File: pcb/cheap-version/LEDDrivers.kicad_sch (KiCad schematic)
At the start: 54 parts, among them J711 LED +/- (return isolated), J721 LED +/- (return isolated), J731 LED +/- (return isolated), Q711 AOD66923, Q721 AOD66923, U700 SN74LVC1G08DBVR, U710 AL8853S-13, U720 AL8853S-13

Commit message: cheap-version: schematic substitutions from stock parts
tools/make_cheap1.py generates the cheap-1 sheets from the PCB_V1 0.22 baseline:
ST1S14 for LMR16020 (RT resistor removed, EN/FB divider recalculated), IRS4427S and
IRL2505 for the heater, BSC146N10LS5 for the LED boost switches, SS56 diodes,
KF301/FS1.5/KF2510/XH connectors, stock resistors and capacitors (Source field =
stock:<id>). J901 XT60 is replaced by a screw terminal as decided. U101 TPS54202 and
D711/D721 SS5P10 are kept because datasheets for ST1S10 and SBRT15U100SP5 were not
available. ERC: 0 errors (one warning: footprint for the DTMSS-27 inductor pending);
netdiff against PCB_V1: no connectivity differences among untouched pins.

Co-Authored-By: Claude Sonnet 5.5 <noreply@anthropic.com>
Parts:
- C700: Source (none) -> stock:54
- C710, C715, C725: LCSC C386166 -> C92388; MPN UMK325AB7106KMHP -> CL32B106KBJNNNE; Manufacturer Taiyo Yuden -> Samsung Electro-Mechanics; Source (none) -> stock:47
- C711, C721: value 1u 50V X7R -> 2.2u 50V X7R; footprint Capacitor_SMD:C_0805_2012Metric -> Capacitor_SMD:C_1206_3216Metric; LCSC C28323 -> (none); MPN CL21B105KBFNNNE -> 12065C225KATM-HW; Manufacturer Samsung -> KYOCERA AVX; Source (none) -> stock:3
- C716, C717, C718, C719, C726, C727, C728: value 10u 100V X7S -> 4.7u 100V X7R; LCSC C576517 -> (none); MPN GRM32EC72A106KE05L -> CL32B475KCI6PJE; Manufacturer Murata -> Samsung Electro-Mechanics; Source (none) -> stock:2
- J711, J721, J731: footprint GrowBox:TerminalBlock_KANGNEX_WJ500V-5.08_1x02_P5.08mm_Horizontal -> TerminalBlock_Phoenix:TerminalBlock_Phoenix_MKDS-1,5-2_1x02_P5.00mm_Horizontal; LCSC C8465 -> (none); MPN WJ500V-5.08-2P -> KF301-5.0-2P; Manufacturer KANGNEX -> (none); Source (none) -> stock:93
- L711: value 47u SRP1770TA-470M -> 47u DTMSS-27/0.047/15-V; footprint Inductor_SMD:L_Bourns_SRP1770TA_16.9x16.9mm -> GrowBox:L_Feryster_DTMSS-27_THT; LCSC C2041872 -> (none); MPN SRP1770TA-470M -> DTMSS-27/0.047/15-V; Manufacturer Bourns -> Feryster; Source (none) -> stock:12
- Q711, Q721: value AOD66923 -> BSC146N10LS5; footprint GrowBox:TO-252-2_NMOS_S123_G4_D5 -> Package_TO_SOT_SMD:TDSON-8-1; symbol GrowBox:AOD66923 -> GrowBox:BSC146N10LS5; LCSC C485687 -> (none); MPN AOD66923 -> BSC146N10LS5; Manufacturer AOS -> Infineon Technologies; Source (none) -> stock:112
- R703: footprint Resistor_SMD:R_0603_1608Metric -> Resistor_SMD:R_1206_3216Metric; LCSC C105579 -> (none); MPN RC0603FR-0747KL -> (none); Manufacturer Yageo -> (none); Source (none) -> stock:61
- R711, R721: value 10R -> 10R 5%; footprint Resistor_SMD:R_0603_1608Metric -> Resistor_SMD:R_1206_3216Metric; Source (none) -> stock:41
- R712: MPN 0603WAF1001T5E -> RC0603FR-071KL; Manufacturer UNI-ROYAL -> Yageo; Source (none) -> stock:62
- R713, R723: LCSC C25803 -> C14675; MPN 0603WAF1003T5E -> RC0603FR-07100KL; Manufacturer UNI-ROYAL -> Yageo; Source (none) -> stock:55
- R714, R724: value 10k / comp tune -> 10k 5%; footprint Resistor_SMD:R_0603_1608Metric -> Resistor_SMD:R_0805_2012Metric; Source (none) -> stock:70
- R718, R728: footprint Resistor_SMD:R_0603_1608Metric -> Resistor_SMD:R_0805_2012Metric; Source (none) -> stock:59

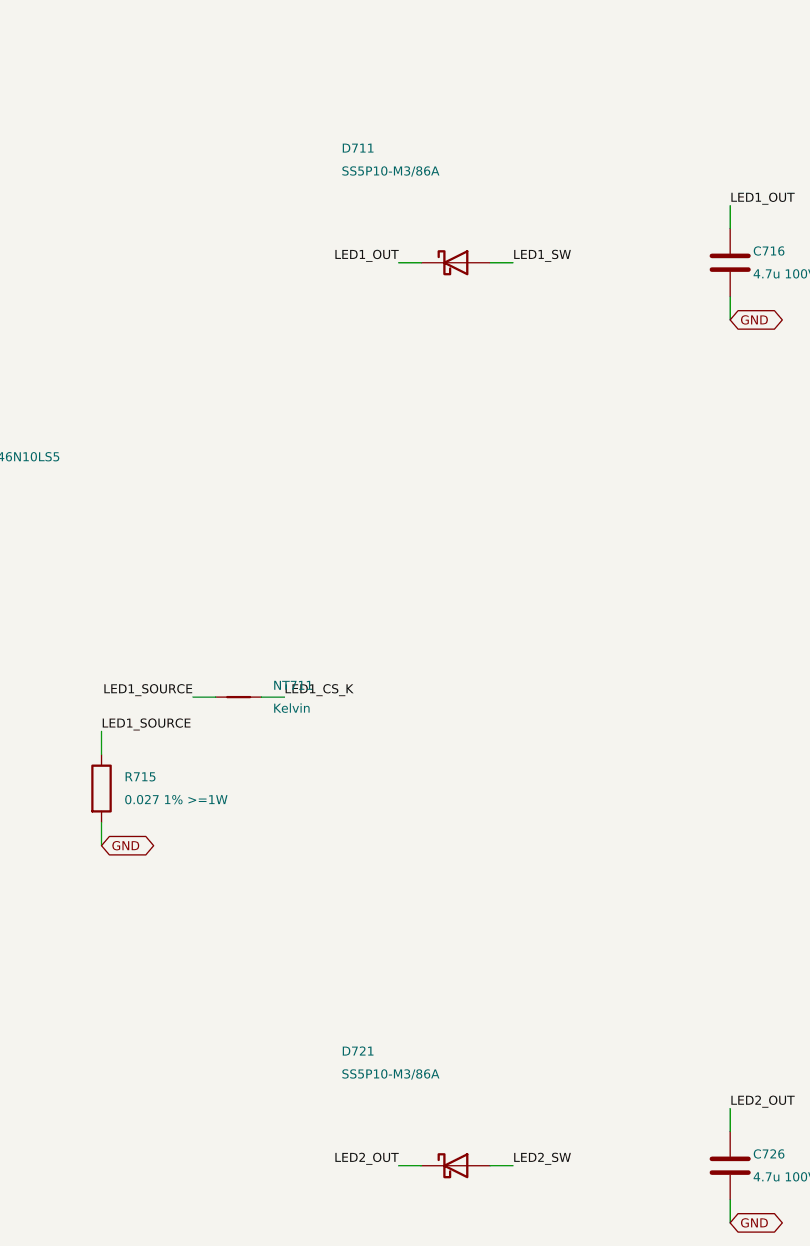
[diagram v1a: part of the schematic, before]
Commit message: cheap-version: ST1S10, SBRT15U100SP5, datasheet checks, LED boost estimate
With the datasheets supplied by the user: U101 TPS54202 -> ST1S10PHR (INH to VIN, SYNC to GND,
L101 4.7 uH FXL0630-4R7-M, R102 31.6k, C103 repurposed as the VIN_A bypass); the 3.3 V sheet is
redrawn in the stub-and-label style. D711/D721 -> SBRT15U100SP5 with a new GrowBox:Diodes_PowerDI5
footprint (tools/make_footprints.py). IRS4427S pinout/levels, BSC146N10LS5 and DTMSS-27 data
checked; tools/analyze_led_cheap.py re-runs the PCB_V1 LED boost model with the stock parts
(all checks pass). Datasheet PDFs are not committed (datasheets/.gitignore). ERC: 0 errors,
only the pending DTMSS-27 footprint warning; netdiff vs PCB_V1: no differences.

Co-Authored-By: Claude Sonnet 5.5 <noreply@anthropic.com>
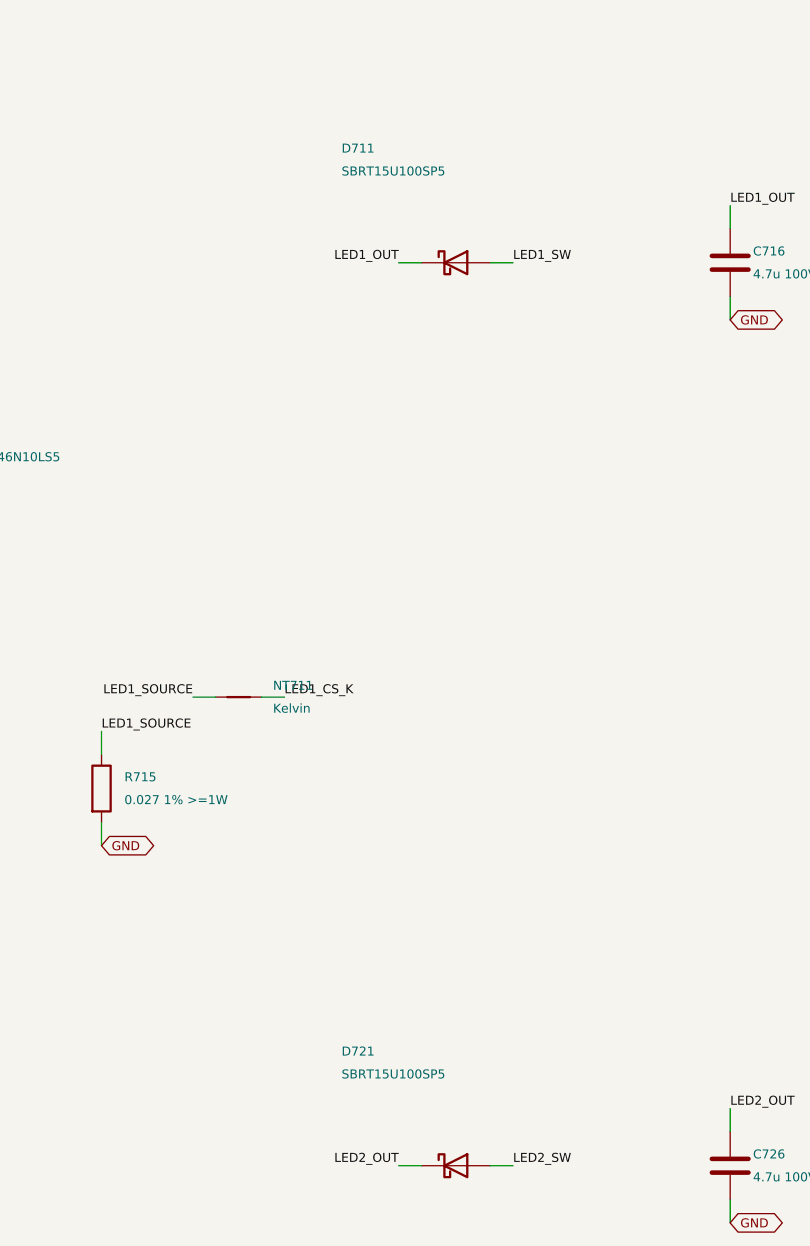
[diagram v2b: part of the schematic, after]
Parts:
- D711, D721: value SS5P10-M3/86A -> SBRT15U100SP5; footprint GrowBox:Vishay_TO-277A_D_K1_A2 -> GrowBox:Diodes_PowerDI5; LCSC C46986 -> C2934601; MPN SS5P10-M3/86A -> SBRT15U100SP5-13; Manufacturer Vishay -> Diodes Incorporated; Source (none) -> stock:8
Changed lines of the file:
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@@
 			)
 		)
-		(property "Value" "SS5P10-M3/86A"
+		(property "Value" "SBRT15U100SP5"
 			(at 276.86 187.96 0)
 			(show_name no)
@@
 			)
 		)
-		(property "Footprint" "GrowBox:Vishay_TO-277A_D_K1_A2"
+		(property "Footprint" "GrowBox:Diodes_PowerDI5"
 			(at 289.56 198.12 0)
 			(hide yes)
@@
 			)
 		)
-		(property "Datasheet" "https://www.vishay.com/docs/88984/ss5p10.pdf"
+		(property "Datasheet" "https://www.diodes.com/assets/Datasheets/SBRT15U100SP5.pdf"
 			(at 289.56 198.12 0)
 			(hide yes)
@@
 			)
 		)
-		(property "Manufacturer" "Vishay"
+		(property "Manufacturer" "Diodes Incorporated"
 			(at 289.56 198.12 0)
 			(hide yes)
@@
 			)
 		)
-		(property "MPN" "SS5P10-M3/86A"
+		(property "MPN" "SBRT15U100SP5-13"
 			(at 289.56 198.12 0)
 			(hide yes)
@@
 			)
 		)
-		(property "LCSC" "C46986"
+		(property "LCSC" "C2934601"
 			(at 289.56 198.12 0)
 			(hide yes)
@@
 					(size 1 1)
 				)
+				(justify left)
+			)
+		)
+		(property "Source" "stock:8"
+			(at 289.56 198.12 0)
+			(effects
+				(font
+					(size 1 1)
+				)
+				(hide yes)
 				(justify left)
 			)
@@
 			)
 		)
-		(property "Value" "SS5P10-M3/86A"
+		(property "Value" "SBRT15U100SP5"
 			(at 276.86 87.63 0)
 			(show_name no)
@@
 			)
 		)
-		(property "Footprint" "GrowBox:Vishay_TO-277A_D_K1_A2"
+		(property "Footprint" "GrowBox:Diodes_PowerDI5"
 			(at 289.56 97.79 0)
 			(hide yes)
@@
 			)
 		)
-		(property "Datasheet" "https://www.vishay.com/docs/88984/ss5p10.pdf"
+		(property "Datasheet" "https://www.diodes.com/assets/Datasheets/SBRT15U100SP5.pdf"
 			(at 289.56 97.79 0)
 			(hide yes)
@@
 			)
 		)
-		(property "Manufacturer" "Vishay"
+		(property "Manufacturer" "Diodes Incorporated"
 			(at 289.56 97.79 0)
 			(hide yes)
@@
 			)
 		)
-		(property "MPN" "SS5P10-M3/86A"
+		(property "MPN" "SBRT15U100SP5-13"
 			(at 289.56 97.79 0)
 			(hide yes)
@@
 			)
 		)
-		(property "LCSC" "C46986"
+		(property "LCSC" "C2934601"
 			(at 289.56 97.79 0)
 			(hide yes)
@@
 				(justify left)
 			)
+		)
+		(property "Source" "stock:8"
+			(at 289.56 97.79 0)
+			(effects
+				(font
+					(size 1 1)
+				)
+				(hide yes)
+				(justify left)
+			)

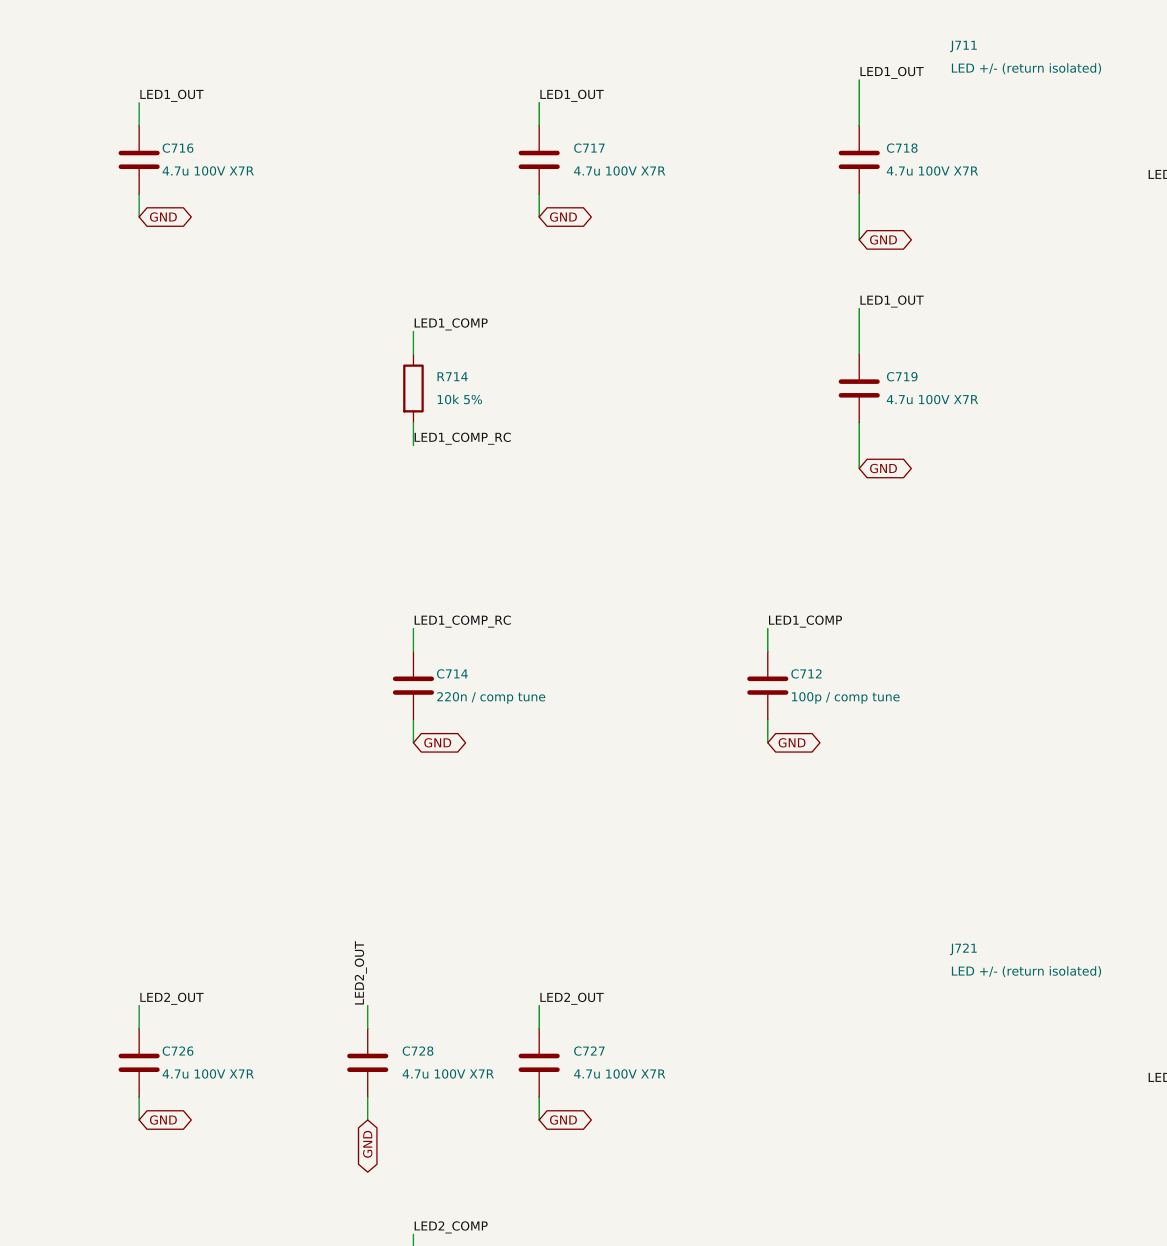
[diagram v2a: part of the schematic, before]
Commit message: cheap-version: DTMSS-27 footprint and 3D, keep X7S output capacitors
Decisions: L711 DTMSS-27/0.047/15-V stands on the board (footprint L_Feryster_DTMSS-27_V from the
Feryster sheet: leads 17.5 mm apart, 2.4 mm drills), output capacitors stay the Murata 10 uF/100 V X7S
as in PCB_V1. Simplified 3D models for the DTMSS-27 and PowerDI5 footprints (tools/make_models3d.py),
LED boost estimate re-run with PCB_V1 capacitor parameters (all checks pass). ERC: 0 violations.

Co-Authored-By: Claude Sonnet 5.5 <noreply@anthropic.com>
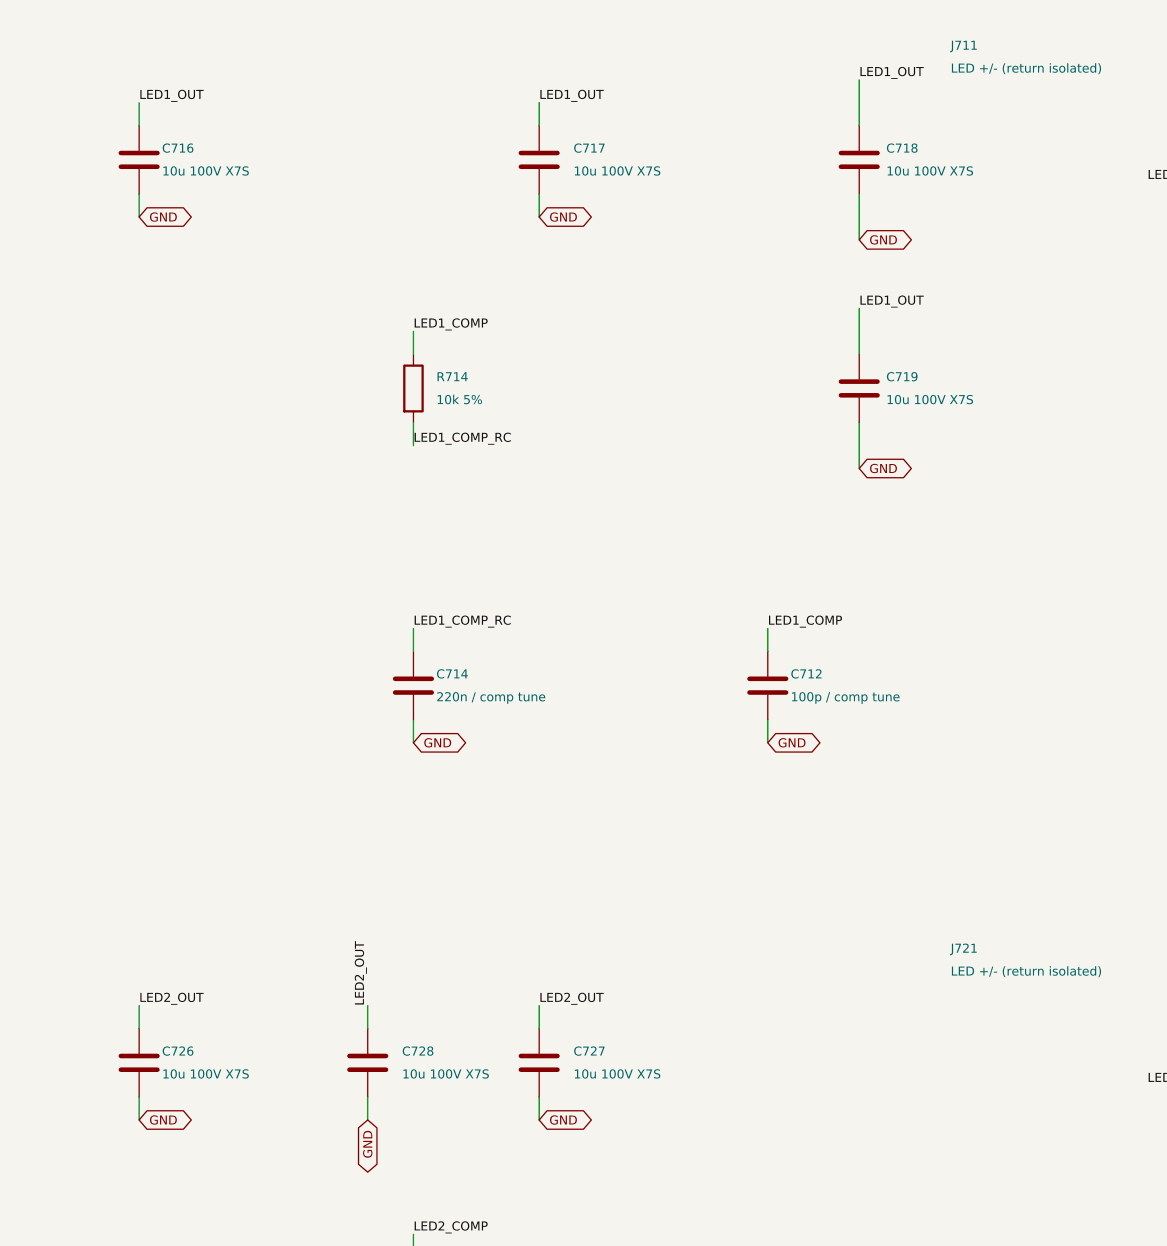
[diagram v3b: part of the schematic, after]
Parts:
- C716, C717, C718, C719, C726, C727, C728: value 4.7u 100V X7R -> 10u 100V X7S; LCSC (none) -> C576517; MPN CL32B475KCI6PJE -> GRM32EC72A106KE05L; Manufacturer Samsung Electro-Mechanics -> Murata; Source stock:2 -> (none)
- L711: footprint GrowBox:L_Feryster_DTMSS-27_THT -> GrowBox:L_Feryster_DTMSS-27_V
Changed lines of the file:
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@@
 			)
 		)
-		(property "Footprint" "GrowBox:L_Feryster_DTMSS-27_THT"
+		(property "Footprint" "GrowBox:L_Feryster_DTMSS-27_V"
 			(at 165.1 97.79 90)
 			(hide yes)
@@
 			)
 		)
-		(property "Value" "4.7u 100V X7R"
+		(property "Value" "10u 100V X7S"
 			(at 322.58 199.39 0)
 			(show_name no)
@@
 			)
 		)
-		(property "Manufacturer" "Samsung Electro-Mechanics"
+		(property "Manufacturer" "Murata"
 			(at 320.04 198.12 0)
 			(hide yes)
@@
 			)
 		)
-		(property "MPN" "CL32B475KCI6PJE"
+		(property "MPN" "GRM32EC72A106KE05L"
 			(at 320.04 198.12 0)
 			(hide yes)
@@
 			)
 		)
-		(property "LCSC" ""
+		(property "LCSC" "C576517"
 			(at 320.04 198.12 0)
 			(hide yes)
@@
 			)
 		)
-		(property "Source" "stock:2"
-			(at 320.04 198.12 0)
-			(effects
-				(font
-					(size 1 1)
-				)
-				(hide yes)
-				(justify left)
-			)
-		)
 	)
 	(symbol
@@
 			)
 		)
-		(property "Value" "4.7u 100V X7R"
+		(property "Value" "10u 100V X7S"
 			(at 368.3 199.39 0)
 			(show_name no)
@@
 			)
 		)
-		(property "Manufacturer" "Samsung Electro-Mechanics"
+		(property "Manufacturer" "Murata"
 			(at 364.49 198.12 0)
 			(hide yes)
@@
 			)
 		)
-		(property "MPN" "CL32B475KCI6PJE"
+		(property "MPN" "GRM32EC72A106KE05L"
 			(at 364.49 198.12 0)
 			(hide yes)
@@
 			)
 		)
-		(property "LCSC" ""
+		(property "LCSC" "C576517"
 			(at 364.49 198.12 0)
 			(hide yes)
@@
 			)
 		)
-		(property "Source" "stock:2"
-			(at 364.49 198.12 0)
-			(effects
-				(font
-					(size 1 1)
-				)
-				(hide yes)
-				(justify left)
-			)
-		)
 	)
 	(symbol
@@
 			)
 		)
-		(property "Value" "4.7u 100V X7R"
+		(property "Value" "10u 100V X7S"
 			(at 368.3 99.06 0)
 			(show_name no)
@@
 			)
 		)
-		(property "Manufacturer" "Samsung Electro-Mechanics"
+		(property "Manufacturer" "Murata"
 			(at 364.49 97.79 0)
 			(hide yes)
@@
 			)
 		)
-		(property "MPN" "CL32B475KCI6PJE"
+		(property "MPN" "GRM32EC72A106KE05L"
 			(at 364.49 97.79 0)
 			(hide yes)
@@
 			)
 		)
-		(property "LCSC" ""
+		(property "LCSC" "C576517"
 			(at 364.49 97.79 0)
 			(hide yes)
@@
 			)
 		)
-		(property "Source" "stock:2"
-			(at 364.49 97.79 0)
-			(effects
-				(font
-					(size 1 1)
-				)
-				(hide yes)
-				(justify left)
-			)
-		)
 	)
 	(symbol
@@
 			)
 		)
-		(property "Value" "4.7u 100V X7R"
+		(property "Value" "10u 100V X7S"
 			(at 322.58 99.06 0)
 			(show_name no)
@@
 			)
 		)
-		(property "Manufacturer" "Samsung Electro-Mechanics"
+		(property "Manufacturer" "Murata"
 			(at 320.04 97.79 0)
 			(hide yes)
@@
 			)
 		)
-		(property "MPN" "CL32B475KCI6PJE"
+		(property "MPN" "GRM32EC72A106KE05L"
 			(at 320.04 97.79 0)
 			(hide yes)
@@
 			)
 		)
-		(property "LCSC" ""
+		(property "LCSC" "C576517"
 			(at 320.04 97.79 0)
 			(hide yes)
@@
 			)
 		)
-		(property "Source" "stock:2"
-			(at 320.04 97.79 0)
-			(effects
-				(font
-					(size 1 1)
-				)
-				(hide yes)
-				(justify left)
-			)
-		)
 	)
 	(symbol
@@
 			)
 		)
-		(property "Value" "4.7u 100V X7R"
+		(property "Value" "10u 100V X7S"
 			(at 403.05 99.06 0)
 			(effects
@@
 			)
 		)
-		(property "Manufacturer" "Samsung Electro-Mechanics"
+		(property "Manufacturer" "Murata"
 			(at 400.05 97.79 0)
 			(effects
@@
 			)
 		)
-		(property "MPN" "CL32B475KCI6PJE"
+		(property "MPN" "GRM32EC72A106KE05L"
 			(at 400.05 97.79 0)
 			(effects
@@
 			)
 		)
-		(property "LCSC" ""
-			(at 400.05 97.79 0)
-			(effects
-				(font
-					(size 1 1)
-				)
-				(hide yes)
-				(justify left)
-			)
-		)
-		(property "Source" "stock:2"
+		(property "LCSC" "C576517"
 			(at 400.05 97.79 0)
 			(effects
@@
 			)
 		)
-		(property "Value" "4.7u 100V X7R"
+		(property "Value" "10u 100V X7S"
 			(at 403.05 124.46 0)
 			(effects
@@
 			)
 		)
-		(property "Manufacturer" "Samsung Electro-Mechanics"
-			(at 400.05 123.19 0)
-			(effects
-				(font
-					(size 1 1)
-				)
-				(hide yes)
-				(justify left)
-			)
-		)
-		(property "MPN" "CL32B475KCI6PJE"
+		(property "Manufacturer" "Murata"
 			(at 400.05 123.19 0)
 			(effects
@@
 			)
 		)
-		(property "LCSC" ""
+		(property "MPN" "GRM32EC72A106KE05L"
 			(at 400.05 123.19 0)
 			(effects
@@
 			)
 		)
-		(property "Source" "stock:2"
+		(property "LCSC" "C576517"
 			(at 400.05 123.19 0)
 			(effects
@@
 			)
 		)
-		(property "Value" "4.7u 100V X7R"
+		(property "Value" "10u 100V X7S"
 			(at 349.25 199.39 0)
 			(effects
@@
 			)
 		)
-		(property "Manufacturer" "Samsung Electro-Mechanics"
+		(property "Manufacturer" "Murata"
 			(at 345.44 198.12 0)
 			(effects
@@
 			)
 		)
-		(property "MPN" "CL32B475KCI6PJE"
-			(at 345.44 198.12 0)
-			(effects
-				(font
-					(size 1 1)
-				)
-				(hide yes)
-				(justify left)
-			)
-		)
-		(property "LCSC" ""
+		(property "MPN" "GRM32EC72A106KE05L"
 			(at 345.44 198.12 0)
 			(effects
@@
 			)
 		)
-		(property "Source" "stock:2"
+		(property "LCSC" "C576517"
 			(at 345.44 198.12 0)
 			(effects
